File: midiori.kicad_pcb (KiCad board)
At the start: 2 copper layers, 140 x 150 mm, 54 parts, among them J1 x68000_expansion, J2 DIN-5_180degree, J3 DIN-5_180degree, J4 DIN-5_180degree, U1 74LS245, U10 74LS393, U11 74LS74, U12 74LS30, U13 H11L1, U14 74LS07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

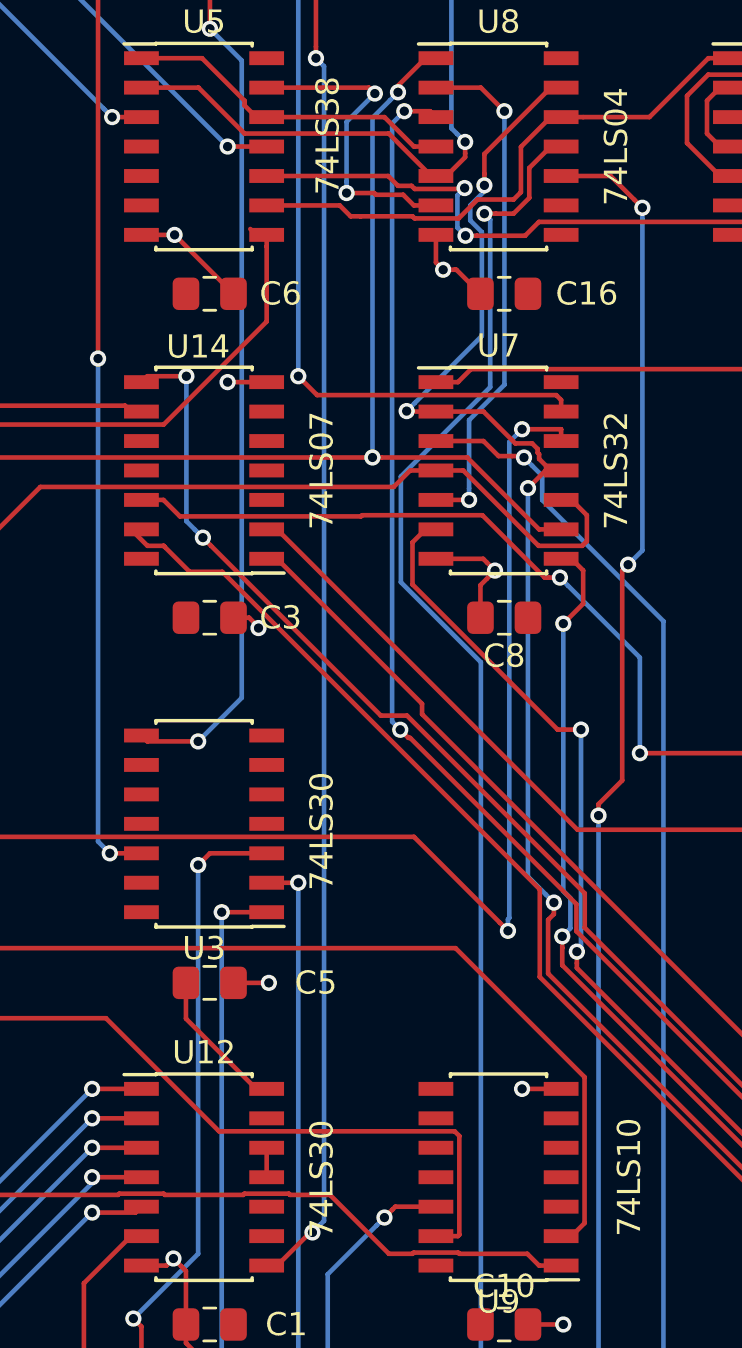
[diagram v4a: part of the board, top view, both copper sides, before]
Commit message: ground unused inputs
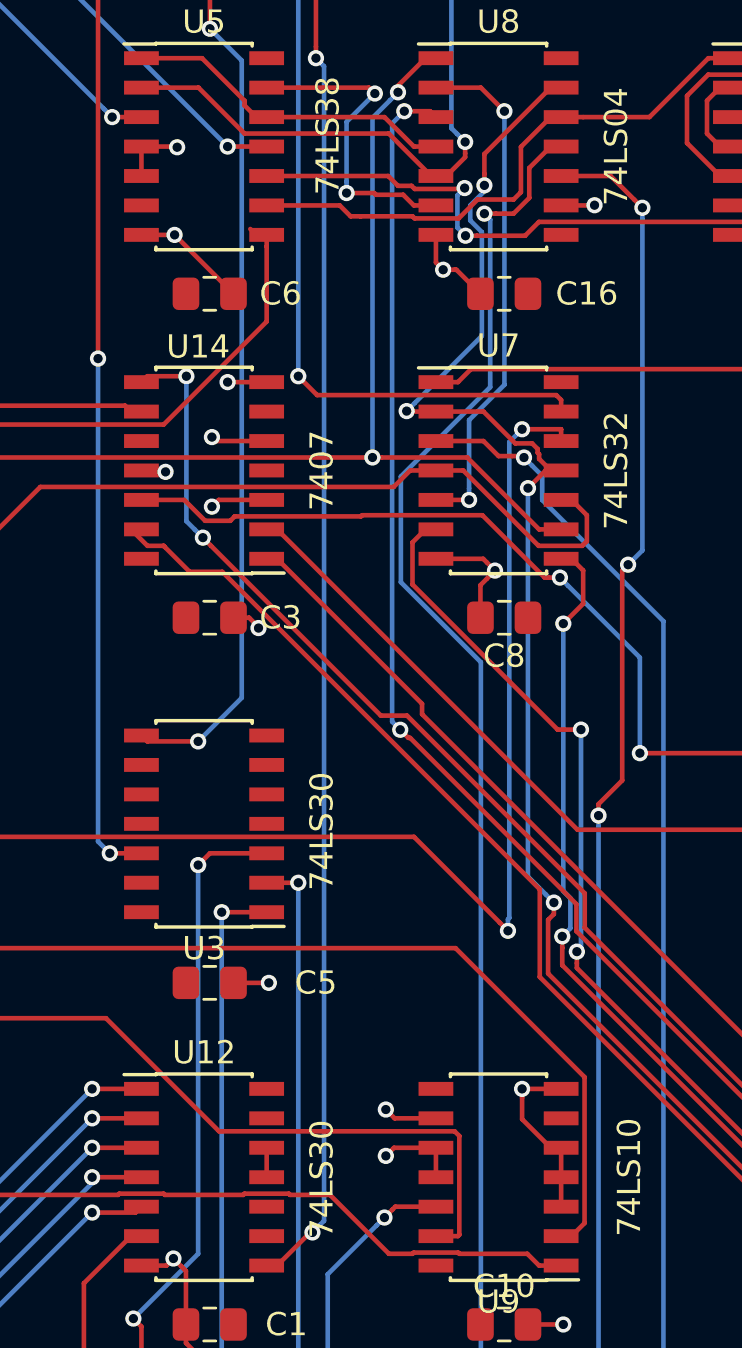
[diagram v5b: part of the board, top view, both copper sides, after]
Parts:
- U14: value 74LS07 -> 7407
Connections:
- U14 pad 10: (no net) -> Net-(U14-Pad10)
- U14 pad 11: (no net) -> GND
- U14 pad 3: (no net) -> GND
- U14 pad 4: (no net) -> Net-(U14-Pad4)
- U14 pad 5: (no net) -> GND
- U14 pad 6: (no net) -> Net-(U14-Pad6)
- U5 pad 4: (no net) -> GND
- U5 pad 5: (no net) -> GND
- U5 pad 6: (no net) -> Net-(U5-Pad6)
- U8 pad 8: (no net) -> Net-(U8-Pad8)
- U8 pad 9: (no net) -> GND
- U9 pad 10: (no net) -> GND
- U9 pad 11: (no net) -> GND
- U9 pad 3: (no net) -> GND
- U9 pad 4: (no net) -> GND
- U9 pad 5: (no net) -> GND
- U9 pad 6: (no net) -> Net-(U9-Pad6)
- U9 pad 8: (no net) -> Net-(U9-Pad8)
- U9 pad 9: (no net) -> GND
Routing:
- net GND: track 170.6 -> 192.7 mm, vias 27 -> 34
- net +5V: track 39.6 -> 33.8 mm

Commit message: rev1
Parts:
- added J5: AudioJack3, Connector_Audio:Jack_3.5mm_CUI_SJ1-3533NG_Horizontal, F.Cu at (183.0, 135.0)
- added J6: AudioJack3, Connector_Audio:Jack_3.5mm_CUI_SJ1-3533NG_Horizontal, F.Cu at (183.0, 75.0)
- added J7: AudioJack3, Connector_Audio:Jack_3.5mm_CUI_SJ1-3533NG_Horizontal, F.Cu at (183.0, 105.0)
- moved J2 10.0 mm to (172.0, 90.0)
- moved J3 5.00 mm to (172.0, 120.0)
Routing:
- net Net-(J2-Pad5): track 15.6 -> 41.6 mm
- net Net-(J4-Pad5): track 26.4 -> 49.0 mm
- net Net-(J3-Pad5): track 17.9 -> 38.4 mm
- net Net-(J2-Pad4): track 15.5 -> 29.7 mm
- net Net-(J4-Pad4): track 24.0 -> 34.9 mm
- net Net-(J3-Pad4): track 15.9 -> 26.3 mm

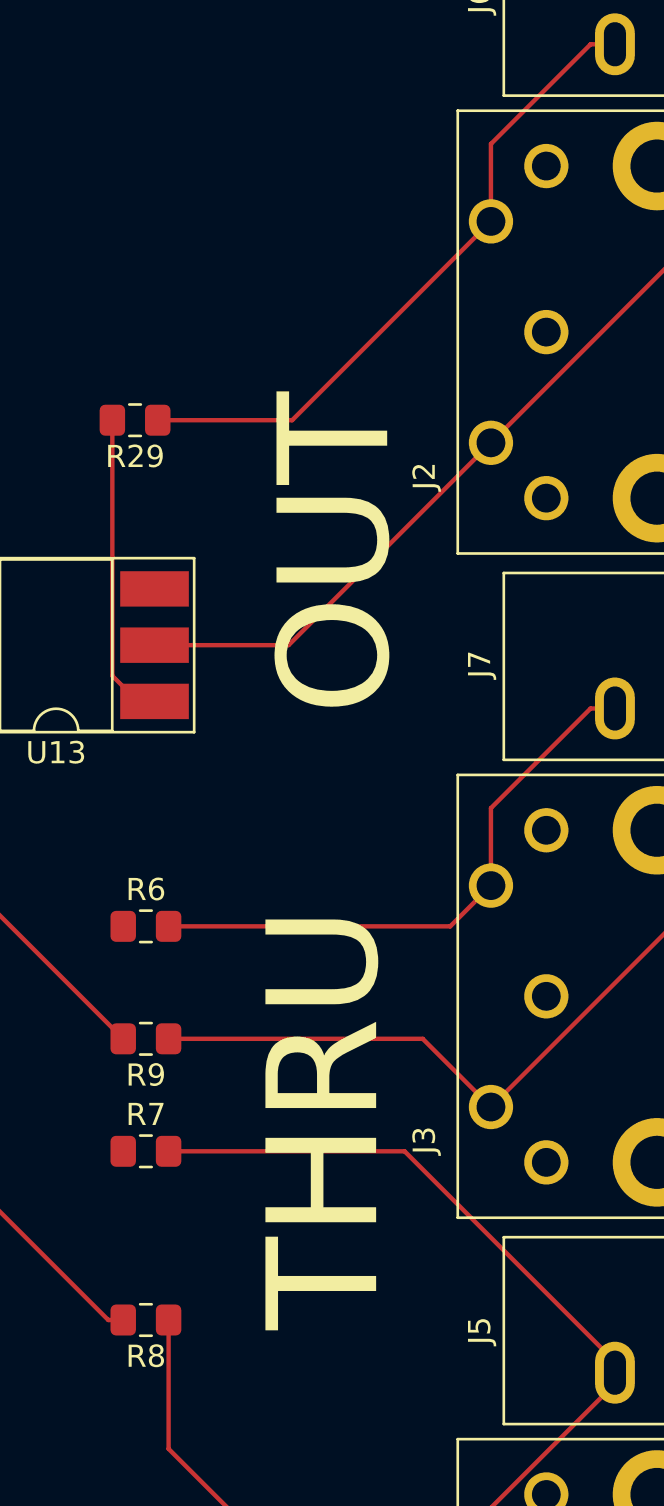
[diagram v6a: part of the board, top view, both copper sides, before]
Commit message: Move IN THRU OUT labels
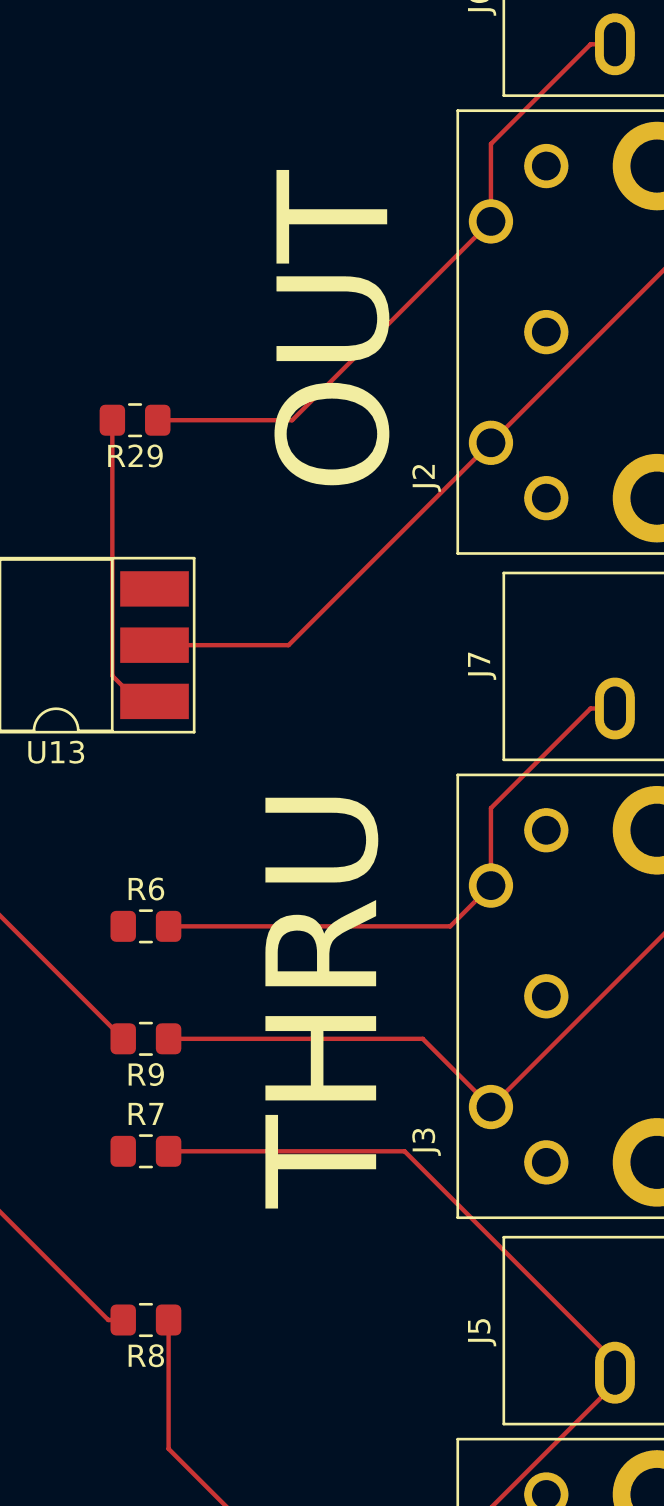
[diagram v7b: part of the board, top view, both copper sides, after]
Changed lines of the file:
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@@
   )
   (gr_poly (pts (xy 83.058 132.08) (xy 86.868 132.08) (xy 86.868 132.842) (xy 83.058 132.842)) (layer F.SilkS) (width 0.1))
-  (gr_text OUT (at 162.5 100 90) (layer F.SilkS)
+  (gr_text OUT (at 162.5 90 90) (layer F.SilkS)
     (effects (font (size 5 5) (thickness 0.15)))
   )
-  (gr_text THRU (at 162 125.5 90) (layer F.SilkS)
+  (gr_text THRU (at 162 120 90) (layer F.SilkS)
     (effects (font (size 5 5) (thickness 0.15)))
   )

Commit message: bugfixes
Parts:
- moved C14 8.06 mm to (146.2, 111.2), turned to 0 degrees
- moved REF** 2.00 mm to (181.0, 172.0)
- moved REF** 2.00 mm to (181.0, 182.0)
- moved R5 1.34 mm to (107.8, 77.0), turned to 180 degrees
- moved C1 0.52 mm to (74.0, 127.8)
- moved J1 0.46 mm to (50.0, 173.5)
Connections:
- J1 pad B22: /A16 -> /AB16
- J1 pad B23: /A17 -> /AB17
- J1 pad B24: /A18 -> /AB18
- J1 pad B25: /A19 -> /AB19
- J1 pad B26: /A20 -> /AB20
- J1 pad B27: /A21 -> /AB21
- J1 pad B28: /A22 -> /AB22
- J1 pad B29: /A23 -> /AB23
- U14 pad 11: GND -> Net-(U14-Pad11)
- U14 pad 3: GND -> Net-(U14-Pad11)
- U14 pad 5: GND -> Net-(U14-Pad11)
- U3 pad 14: (no net) -> +5V
- U3 pad 7: (no net) -> GND
- U4 pad 10: Net-(U3-Pad8) -> GND
- U4 pad 9: Net-(U4-Pad11) -> Net-(U14-Pad11)
- U7 pad 13: Net-(U4-Pad8) -> Net-(U4-Pad11)
- U8 pad 8: Net-(U8-Pad8) -> Net-(U12-Pad11)
- U8 pad 9: GND -> Net-(U3-Pad8)
- U9 pad 10: GND -> Net-(U14-Pad11)
- U9 pad 11: GND -> Net-(U14-Pad11)
- U9 pad 3: GND -> Net-(U14-Pad11)
- U9 pad 4: GND -> Net-(U14-Pad11)
- U9 pad 5: GND -> Net-(U14-Pad11)
- U9 pad 9: GND -> Net-(U14-Pad11)
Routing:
- net Net-(U14-Pad11): track 0.00 -> 79.5 mm, vias 0 -> 7
- net /AB23: track 0.00 -> 58.6 mm, vias 0 -> 3
- net Net-(U12-Pad11): track 1.27 -> 56.8 mm, vias 0 -> 2
- net /AB18: track 0.00 -> 45.1 mm, vias 0 -> 1
- net /AB20: track 0.00 -> 39.4 mm, vias 0 -> 1
- net /AB19: track 0.00 -> 38.0 mm, vias 0 -> 3
- net Net-(U4-Pad8): track 33.5 -> 0.00 mm, vias 2 -> 0
- net /AB17: track 0.00 -> 33.5 mm, vias 0 -> 3
- net Net-(U4-Pad11): track 3.90 -> 37.4 mm, vias 0 -> 2
- net /AB16: track 0.00 -> 33.4 mm, vias 0 -> 3
- net /AB21: track 0.00 -> 27.1 mm, vias 0 -> 1
- net /AB22: track 0.00 -> 26.7 mm, vias 0 -> 1
- net /10MHz: track 135.9 -> 151.2 mm, vias 1 -> 3
- net GND: track 192.7 -> 182.5 mm, vias 34 -> 30
- net Net-(U3-Pad8): track 43.5 -> 51.0 mm
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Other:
- outline, holes or cut-outs redrawn
- board text added: "1.1 2019 CC0 TD-Linux https://github.com/tdaede/midiori"
- board text removed: "1.0 2018 CC0 TD-Linux https://github.com/tdaede/midiori"
